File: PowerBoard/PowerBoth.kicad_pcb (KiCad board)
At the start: 2 copper layers, 141.8 x 24.9 mm, 48 parts, among them J201 PJ-079AH, J202 2MM-1X5, J302 2X10-2MMSMD, M201 IRF7205, M301 MOSFET_NSI4778DY, Q201 IRF7205, U201 LTC4002ES8-4.2PBFSO-8_S-M, U301 LM3488

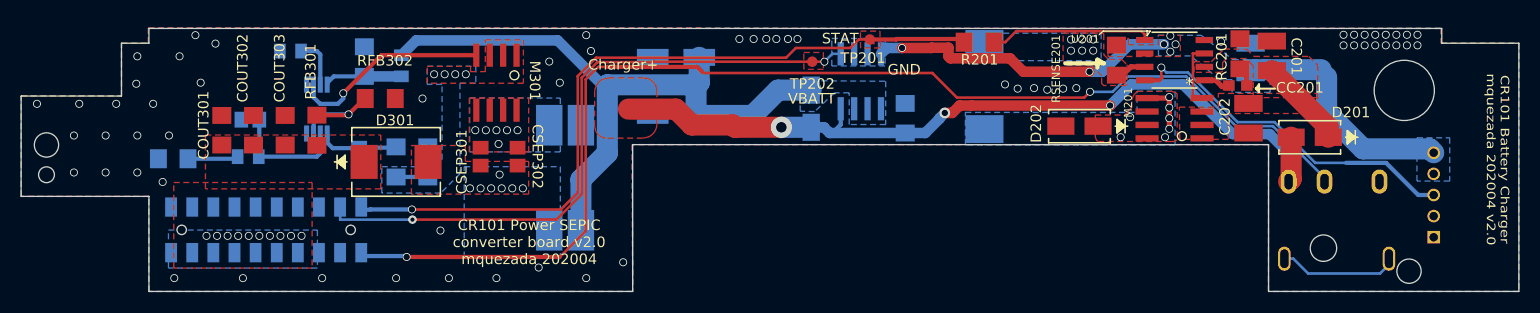
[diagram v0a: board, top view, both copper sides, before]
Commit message: Switch connector model. Reduce silk screen text size.
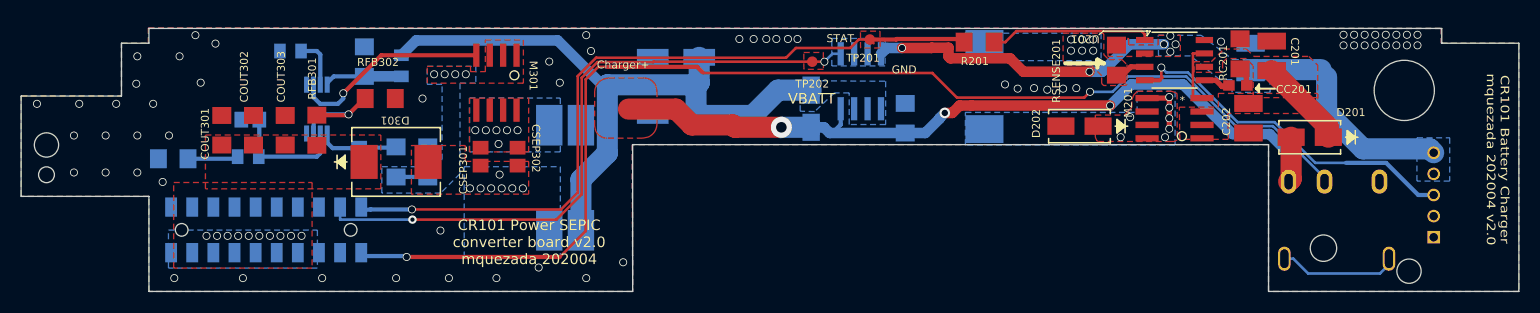
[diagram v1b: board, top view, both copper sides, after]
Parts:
- J302: footprint PowerBoard-Boost-v2:2X10-2MM -> MarcoK:2X10-2MM

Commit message: Separating the power board branch.
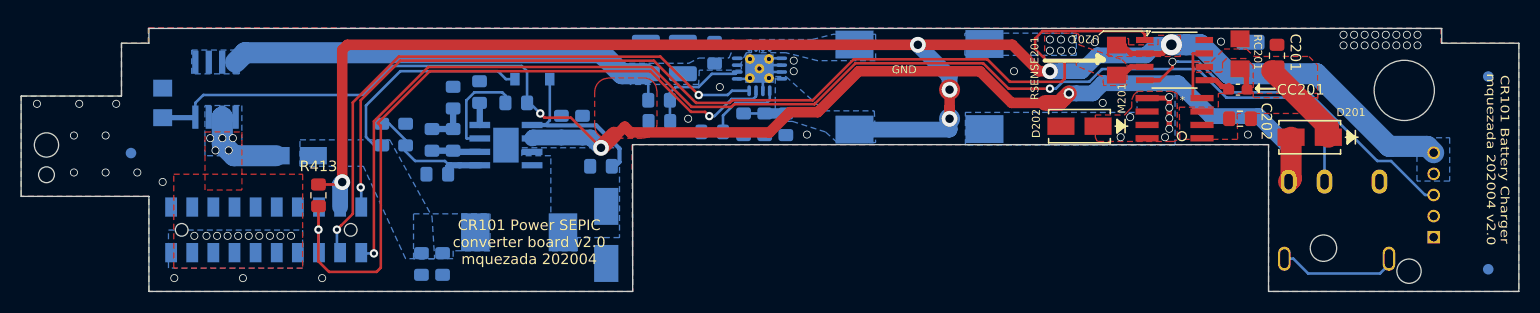
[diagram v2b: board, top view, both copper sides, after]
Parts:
- removed CBP301: 0.1uF, PowerBoard-Boost-v2:C1206
- removed CCOMP301: 15nF, PowerBoard-Boost-v2:C0805
- removed CCOMP302: 0.47uF, PowerBoard-Boost-v2:C1206
- removed CFILT301: 1.5nF, PowerBoard-Boost-v2:C0805
- removed CIN301, CIN302: 3.3uF, PowerBoard-Boost-v2:153CLV-0505
- removed COUT301, COUT302, COUT303: 47uF, PowerBoard-Boost-v2:C1206
- removed CSEP301, CSEP302: 3.3uF, PowerBoard-Boost-v2:C0805
- removed D203: B330A-13, PowerBoard:SMA-M
- removed J302: 2X10-2MMSMD, MarcoK:2X10-2MM
- removed M301: MOSFET_NSI4778DY, PowerBoard-Boost-v2:8SOIC
- removed Q201: IRF7205, PowerBoard:8SOIC
- removed R201: 2K, PowerBoard:R1206
- removed R202: 56K, PowerBoard:1206
- removed RBP301: 20, PowerBoard-Boost-v2:R0805
- removed RCOMP301: 215, PowerBoard-Boost-v2:R0805
- removed RFADJ301: 76.8K, PowerBoard-Boost-v2:R0805
- removed RFB301: 29.4K, PowerBoard-Boost-v2:R1206
- removed RFB302: 10k, PowerBoard-Boost-v2:R1206
- removed RFILT301: 100, PowerBoard-Boost-v2:R1206
- removed RSENSE301: 0.009, PowerBoard-Boost-v2:R1206
- removed TP201, TP202: TEST_POINTROUND-1MM, PowerBoard:TEST_POINT_ROUND_1MM
- removed TP301: Charger+, PowerBoard-Boost-v2:TEST_POINT_ROUND_1MM
- added C1A301: 6.8uF, Capacitor_SMD:C_0805_2012Metric_Pad1.15x1.40mm_HandSolder, B.Cu at (185.2, 130.2)
- added C1B301: 6.8uF, Capacitor_SMD:C_0805_2012Metric_Pad1.15x1.40mm_HandSolder, B.Cu at (187.2, 130.2)
- added C2A301: 10uF, Capacitor_SMD:C_0805_2012Metric_Pad1.15x1.40mm_HandSolder, B.Cu at (174.0, 143.2)
- added C2B301: 10uF, Capacitor_SMD:C_0805_2012Metric_Pad1.15x1.40mm_HandSolder, B.Cu at (172.0, 143.2)
- added C301: 0.1uF, Capacitor_SMD:C_0805_2012Metric_Pad1.15x1.40mm_HandSolder, B.Cu at (189.0, 134.0)
- added C302: 0.1uF, Capacitor_SMD:C_0805_2012Metric_Pad1.15x1.40mm_HandSolder, B.Cu at (177.5, 127.0)
- added C3A301: 3.9uF, Capacitor_SMD:C_0805_2012Metric_Pad1.15x1.40mm_HandSolder, B.Cu at (175.0, 131.5)
- added C3B301: 0.01uF, Capacitor_SMD:C_0805_2012Metric_Pad1.15x1.40mm_HandSolder, B.Cu at (173.0, 131.5)
- added C401: 10uF, Capacitor_SMD:C_0805_2012Metric_Pad1.15x1.40mm_HandSolder, B.Cu at (204.5, 130.0)
- added C402: 2.2uF, Capacitor_SMD:C_0805_2012Metric_Pad1.15x1.40mm_HandSolder, B.Cu at (199.8, 123.2)
- added C403: 100uF, Capacitor_SMD:C_1210_3225Metric_Pad1.42x2.65mm_HandSolder, B.Cu at (193.2, 123.8)
- added C404: 0.1uF, Capacitor_SMD:C_0805_2012Metric_Pad1.15x1.40mm_HandSolder, B.Cu at (206.5, 130.0)
- added C406: 100uF, Capacitor_SMD:C_1210_3225Metric_Pad1.42x2.65mm_HandSolder, B.Cu at (196.8, 123.8)
- added Cfb301: 0.1uF, Capacitor_SMD:C_0805_2012Metric_Pad1.15x1.40mm_HandSolder, B.Cu at (173.5, 134.8)
- added D101: B330A-13, PowerBoard:SMA-M, B.Cu at (160.0, 133.0)
- added Dbs301: 1N4148, Diode_SMD:D_SOD-123, B.Cu at (182.5, 125.8)
- added FID401: FIDUCIAL, PowerBoost1000:FIDUCIAL_1MM, B.Cu at (273.0, 143.8)
- added FID402: FIDUCIAL, PowerBoost1000:FIDUCIAL_1MM, B.Cu at (273.0, 125.5)
- added FID403: FIDUCIAL, PowerBoost1000:FIDUCIAL_1MM, B.Cu at (144.5, 132.8)
- added J101: 2X10-2MMSMD, MarcoK:2X10-2MM, B.Cu at (157.3, 140.0)
- added L401: 6.8uH, PowerBoard:IND_B952AS-H-220M=P3, B.Cu at (213.0, 126.5)
- added Q101: IRF7205, PowerBoard:8SOIC, B.Cu at (152.5, 126.8)
- added R101: 56K, PowerBoard:1206, B.Cu at (147.5, 128.0)
- added R301: 100K, Resistor_SMD:R_0805_2012Metric_Pad1.15x1.40mm_HandSolder, B.Cu at (181.0, 128.0)
- added R302: 6.8K, Resistor_SMD:R_0805_2012Metric_Pad1.15x1.40mm_HandSolder, B.Cu at (175.0, 127.5)
- added R303: 10K, Resistor_SMD:R_0805_2012Metric_Pad1.15x1.40mm_HandSolder, B.Cu at (168.2, 131.0)
- added R304: 47K, Resistor_SMD:R_0805_2012Metric_Pad1.15x1.40mm_HandSolder, B.Cu at (170.5, 131.0)
- added R401: 1.87M, Resistor_SMD:R_0805_2012Metric_Pad1.15x1.40mm_HandSolder, B.Cu at (202.5, 130.0)
- added R402: 340K, Resistor_SMD:R_0805_2012Metric_Pad1.15x1.40mm_HandSolder, B.Cu at (199.5, 130.8)
- added R403: 1.87M, Resistor_SMD:R_0805_2012Metric_Pad1.15x1.40mm_HandSolder, B.Cu at (194.5, 127.8)
- added R404: 200K, Resistor_SMD:R_0805_2012Metric_Pad1.15x1.40mm_HandSolder, B.Cu at (194.5, 129.8)
- added R413: 200K, Resistor_SMD:R_0805_2012Metric_Pad1.15x1.40mm_HandSolder, F.Cu at (162.2, 136.8)
- added U401: TPS61030RSAR, PowerBoost1000:PVQFN-16, B.Cu at (204.0, 124.8)
- C201, C202: footprint PowerBoard:C1210 -> Capacitor_SMD:C_0805_2012Metric_Pad1.15x1.40mm_HandSolder
- C203: footprint PowerBoard:C1210 -> Capacitor_SMD:C_1210_3225Metric_Pad1.42x2.65mm_HandSolder
- CC201: footprint PowerBoard:C0603 -> Capacitor_SMD:C_0603_1608Metric_Pad1.05x0.95mm_HandSolder
- D301: value SL44-E3_57TDIODE_DO214AB-M -> B130; footprint PowerBoard-Boost-v2:DIODE_DO214AB-M -> Diode_SMD:D_SMB_Handsoldering; moved to B.Cu
- L301: value INDUCTOR_DUAL -> 10uH; footprint PowerBoard-Boost-v2:DRQ125 -> Inductor_SMD:L_10.4x10.4_H4.8
- RC201: value R-US_R1206 -> 2.2K
- U301: value LM3488 -> MP2307DN-LF; footprint PowerBoard-Boost-v2:DGK8-M -> Buck:SOIC127P600X170-9N
- moved D301 21.1 mm to (189.5, 140.5), turned to 270 degrees
- moved U301 18.2 mm to (180.0, 132.0), turned to 180 degrees
- moved L301 6.75 mm to (181.2, 140.2), turned to 180 degrees
- moved C202 0.80 mm to (249.5, 129.5), turned to 0 degrees
- moved C201 0.50 mm to (253.0, 123.5)
- moved CC201 0.40 mm to (249.3, 126.8)
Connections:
- net /Charger/VBATT renamed /VBATT
- D201 pad 2: /Charger/V+CH -> /V+CH
- D301 pad 1: 5V -> /MP2307_Buck/SW
- D301 pad 2: /SEPIC Converter/VOUT -> GND
- J201 pad 1: /Charger/V+CH -> /V+CH
- J201 pad 3: /Charger/CHG_CON -> /CHG_CON
- L301 pad 1: /Charger/V+ToBoost -> /MP2307_Buck/SW
- L301 pad 2: /SEPIC Converter/VOUT -> /FromBuck
- U201 pad 5: Net-(R201-Pad1) -> /CHSTAT
- U301 pad 1: /SEPIC Converter/ISEN -> Net-(C301-Pad2)
- U301 pad 2: /SEPIC Converter/COMP -> /V+CH
- U301 pad 3: /SEPIC Converter/FB -> /MP2307_Buck/SW
- U301 pad 5: GND -> /MP2307_Buck/FB
- U301 pad 6: /SEPIC Converter/DR -> Net-(C3A301-Pad1)
- U301 pad 7: /SEPIC Converter/FA -> /EN_BUCK
- U301 pad 8: /SEPIC Converter/VIN -> Net-(C302-Pad1)
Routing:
- net /V+CH: track 0.00 -> 137.1 mm, vias 0 -> 3
- net /CHG_CON: track 0.00 -> 118.5 mm, vias 0 -> 2
- net /Charger/CHG_CON: track 113.5 -> 0.00 mm, vias 2 -> 0
- net /CHSTAT: track 0.00 -> 100.0 mm, vias 0 -> 1
- net /Charger/V+CH: track 78.3 -> 0.00 mm, vias 3 -> 0
- net /Charger/CHSTAT: track 70.7 -> 0.00 mm, vias 1 -> 0
- net /EN_PB: track 0.00 -> 68.6 mm, vias 0 -> 2
- net /Charger/V+ToBoost: track 61.8 -> 0.00 mm
- net /LBO: track 0.00 -> 56.3 mm, vias 0 -> 2
- net /FromBoost: track 0.00 -> 42.6 mm
- net /VBATT: track 113.0 -> 155.4 mm, vias 8 -> 6
- net /FromBuck: track 0.00 -> 20.6 mm
- net /SEPIC Converter/DR: track 19.1 -> 0.00 mm, vias 1 -> 0
- net Net-(C301-Pad2): track 0.00 -> 17.3 mm
- net Net-(R201-Pad1): track 15.5 -> 0.00 mm
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- added copper zone on B.Cu, net /FromBoost
- added copper zone on B.Cu, net /FromBuck
- added copper zone on B.Cu, net /MP2307_Buck/SW
- added copper zone on F.Cu, net /V+CH
- added copper zone on B.Cu, net Net-(L401-Pad1)
- removed copper zone on F.Cu, net /Charger/CHSTAT
- removed copper zone on F.Cu, net /Charger/V+CH
- removed copper zone on B.Cu, net /Charger/V+ToBoost
- removed copper zone on B.Cu, net /SEPIC Converter/SOURCE
- removed copper zone on F.Cu, net /SEPIC Converter/SOURCE
- removed copper zone on B.Cu, net /SEPIC Converter/VIN3
- removed copper zone on F.Cu, net /SEPIC Converter/VIN3
- removed copper zone on B.Cu, net /SEPIC Converter/VOUT
- removed copper zone on F.Cu, net /SEPIC Converter/VOUT
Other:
- outline, holes or cut-outs redrawn
- board text removed: "STAT"
- board text removed: "VBATT"

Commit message: Move mounting holes on PCB closer to correct position.
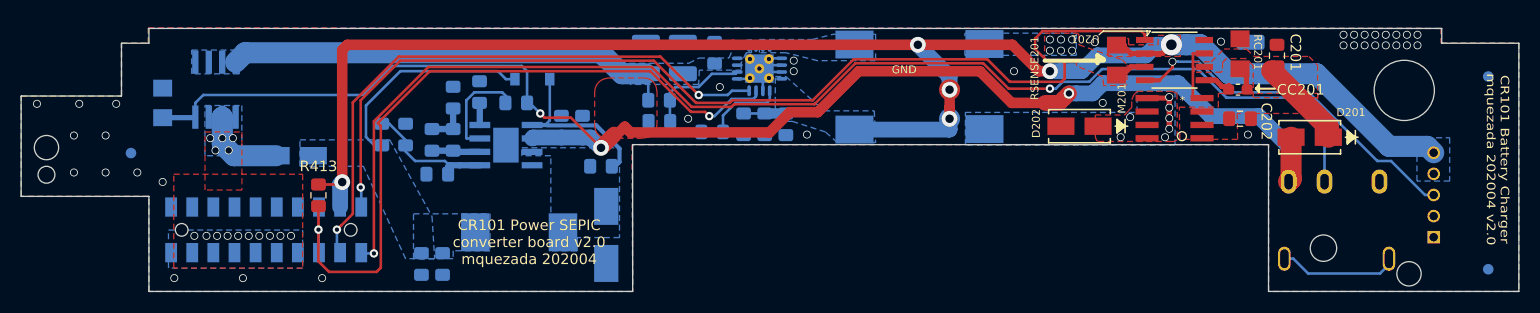
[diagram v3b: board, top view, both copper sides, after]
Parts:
- moved @HOLE2 0.25 mm to (265.5, 144.2)
- moved @HOLE3 0.25 mm to (136.5, 132.2)
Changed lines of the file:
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@@
     (mod_text_size 0.75 0.75)
     (mod_text_width 0.13)
-    (pad_size 1 1)
-    (pad_drill 0)
+    (pad_size 1.6 1.6)
+    (pad_drill 1.6)
     (pad_to_mask_clearance 0.051)
     (solder_mask_min_width 0.25)
@@
   )
   (module "" (layer Top)
-    (at 265.5 143.931209)
+    (at 265.5 144.181209)
     (fp_text reference @HOLE2 (at 0 0 unlocked) (layer F.SilkS) hide
       (effects (font (size 0.75 0.75) (thickness 0.13)))
@@
       (effects (font (size 0.75 0.75) (thickness 0.13)))
     )
-    (pad "" np_thru_hole circle (at 0 0) (size 1.5 1.5) (drill 1.5) (layers *.Cu *.Mask))
+    (pad "" np_thru_hole circle (at 0 0) (size 1.6 1.6) (drill 1.6) (layers *.Cu *.Mask))
   )
   (module "" (layer Top)
-    (at 136.5 131.982262)
+    (at 136.5 132.232262)
     (fp_text reference @HOLE3 (at 0 0 unlocked) (layer F.SilkS) hide
       (effects (font (size 0.75 0.75) (thickness 0.13)))

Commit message: Buck/boost v4.0.
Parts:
- C2A301, C2B301: value 10uF -> 22uF
- C301: value 0.1uF -> 10nF
- C3A301: value 3.9uF -> 3.9nF
- C3B301: value 0.01uF -> (0.01uF)
- D101, Q101, R101: moved to F.Cu
- D301: value B130 -> (B130)
- Dbs301: value 1N4148 -> (1N4148)
- moved L401 63.6 mm to (149.5, 130.8), turned to 180 degrees
- moved C401 53.7 mm to (151.2, 123.2)
- moved C404 53.7 mm to (153.2, 123.2)
- moved U401 46.2 mm to (157.8, 124.8), turned to 90 degrees
- moved C402 41.5 mm to (158.6, 128.9), turned to 180 degrees
- moved C406 40.3 mm to (158.0, 134.8), turned to 180 degrees
- moved R401 39.1 mm to (164.2, 122.2), turned to 0 degrees
- moved C403 36.1 mm to (158.0, 131.5), turned to 180 degrees
- moved R402 35.9 mm to (164.2, 124.2), turned to 180 degrees
- moved R403 31.3 mm to (163.2, 127.2), turned to 270 degrees
- moved R404 29.4 mm to (165.2, 127.2), turned to 90 degrees
- moved R101 22.0 mm to (169.5, 128.8), turned to 180 degrees
- moved Q101 14.6 mm to (165.5, 133.5), turned to 90 degrees
- moved D101 11.9 mm to (170.2, 139.0)
- moved R413 11.5 mm to (163.2, 125.2), turned to 90 degrees
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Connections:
- net Net-(L401-Pad1) renamed /PowerBoost1000/SW
- net Net-(R401-Pad1) renamed /PowerBoost1000/LBI
- net Net-(R403-Pad1) renamed /PowerBoost1000/FB
- R413 pad 1: /VBATT -> /EN_PB
- R413 pad 2: /EN_PB -> /VBATT
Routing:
- net /EN_PB: track 68.6 -> 27.5 mm
- net /FromBoost: track 42.6 -> 3.88 mm, vias 0 -> 4
- net /LBO: track 56.3 -> 28.7 mm
- net /V+CH: track 137.1 -> 119.2 mm, vias 3 -> 4
- net 5V: track 8.10 -> 18.9 mm, vias 15 -> 10
- net GND: track 13.7 -> 4.51 mm, vias 38 -> 89
- net /VBATT: track 155.4 -> 148.6 mm, vias 6 -> 5
- net /CHSTAT: track 100.0 -> 96.9 mm
- net /PowerBoost1000/FB: track 9.94 -> 7.64 mm
- net /PowerBoost1000/LBI: track 9.54 -> 10.3 mm
- net /FromBuck: track 20.6 -> 20.5 mm, vias 0 -> 8
- added copper zone on F.Cu, net /FromBoost
- added copper zone on F.Cu, net /FromBuck
- added copper zone on B.Cu, net GNDPWR
- added copper zone on F.Cu, net GNDPWR
- removed copper zone on F.Cu, net /V+CH
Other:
- board text added: "CR101 Power SEPIC converter board v4.0 mquezada 202006"
- board text removed: "CR101 Power SEPIC converter board v2.0 mquezada 202004"

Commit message: Sending v4.0 with new booster layout and fixed feedback resistors on buck converter.
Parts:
- moved R303 2.25 mm to (170.5, 131.0)
- moved R304 2.25 mm to (168.2, 131.0)
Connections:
- R303 pad 1: /MP2307_Buck/FB -> GND
- R303 pad 2: /FromBuck -> /MP2307_Buck/FB
- R304 pad 1: /MP2307_Buck/FB -> /FromBuck
- R304 pad 2: GND -> /MP2307_Buck/FB
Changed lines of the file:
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@@
   (page A4)
   (layers
-    (0 Top signal)
+    (0 Top signal hide)
     (31 Bottom signal)
     (32 B.Adhes user hide)
@@
   )
   (module Resistor_SMD:R_0805_2012Metric_Pad1.15x1.40mm_HandSolder (layer Bottom)
-    (at 168.25 131 270)
+    (at 170.5 131 270)
     (descr "Resistor SMD 0805 (2012 Metric), square (rectangular) end terminal, IPC_7351 nominal with elongated pad for handsoldering. (Body size source: https://docs.google.com/spreadsheets/d/1BsfQQcO9C6DZCsRaXUlFlo91Tg2WpOkGARC1WS5S8t0/edit?usp=sharing), generated with kicad-footprint-generator")
     (tags "resistor handsolder")
@@
     )
     (pad 1 smd roundrect (at -1.025 0 270) (size 1.15 1.4) (layers Bottom B.Paste B.Mask) (roundrect_rratio 0.217391)
+      (net 1 GND))
+    (pad 2 smd roundrect (at 1.025 0 270) (size 1.15 1.4) (layers Bottom B.Paste B.Mask) (roundrect_rratio 0.217391)
       (net 18 /MP2307_Buck/FB))
-    (pad 2 smd roundrect (at 1.025 0 270) (size 1.15 1.4) (layers Bottom B.Paste B.Mask) (roundrect_rratio 0.217391)
-      (net 25 /FromBuck))
     (model ${KISYS3DMOD}/Resistor_SMD.3dshapes/R_0805_2012Metric.wrl
       (at (xyz 0 0 0))
@@
   )
   (module Resistor_SMD:R_0805_2012Metric_Pad1.15x1.40mm_HandSolder (layer Bottom)
-    (at 170.5 131 90)
+    (at 168.25 131 90)
     (descr "Resistor SMD 0805 (2012 Metric), square (rectangular) end terminal, IPC_7351 nominal with elongated pad for handsoldering. (Body size source: https://docs.google.com/spreadsheets/d/1BsfQQcO9C6DZCsRaXUlFlo91Tg2WpOkGARC1WS5S8t0/edit?usp=sharing), generated with kicad-footprint-generator")
     (tags "resistor handsolder")
@@
     (fp_line (start -1 -0.6) (end -1 0.6) (layer B.Fab) (width 0.1))
     (pad 2 smd roundrect (at 1.025 0 90) (size 1.15 1.4) (layers Bottom B.Paste B.Mask) (roundrect_rratio 0.217391)
-      (net 1 GND))
+      (net 18 /MP2307_Buck/FB))
     (pad 1 smd roundrect (at -1.025 0 90) (size 1.15 1.4) (layers Bottom B.Paste B.Mask) (roundrect_rratio 0.217391)
-      (net 18 /MP2307_Buck/FB))
+      (net 25 /FromBuck))
     (model ${KISYS3DMOD}/Resistor_SMD.3dshapes/R_0805_2012Metric.wrl
       (at (xyz 0 0 0))
@@
       (effects (font (size 0.75 0.75) (thickness 0.13)) (justify mirror))
     )
-    (fp_text value 1.87M (at -4.225 0 180) (layer B.Fab)
+    (fp_text value 1.87M (at 0.025 0 180) (layer B.Fab)
       (effects (font (size 1 1) (thickness 0.15)) (justify mirror))
     )
@@
       (effects (font (size 0.75 0.75) (thickness 0.13)) (justify mirror))
     )
-    (fp_text value 340K (at -0.275 2 180) (layer B.Fab)
-      (effects (font (size 1 1) (thickness 0.15)) (justify mirror))
-    )
+    (fp_text value 340K (at -0.025 0 180) (layer B.Fab)
+      (effects (font (size 1 1) (thickness 0.15)) (justify mirror))
+    )
